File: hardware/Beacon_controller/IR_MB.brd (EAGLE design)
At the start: 50.8 x 50.8 mm, 9 parts, among them U1 ATTINY84ATTINY84-20MU

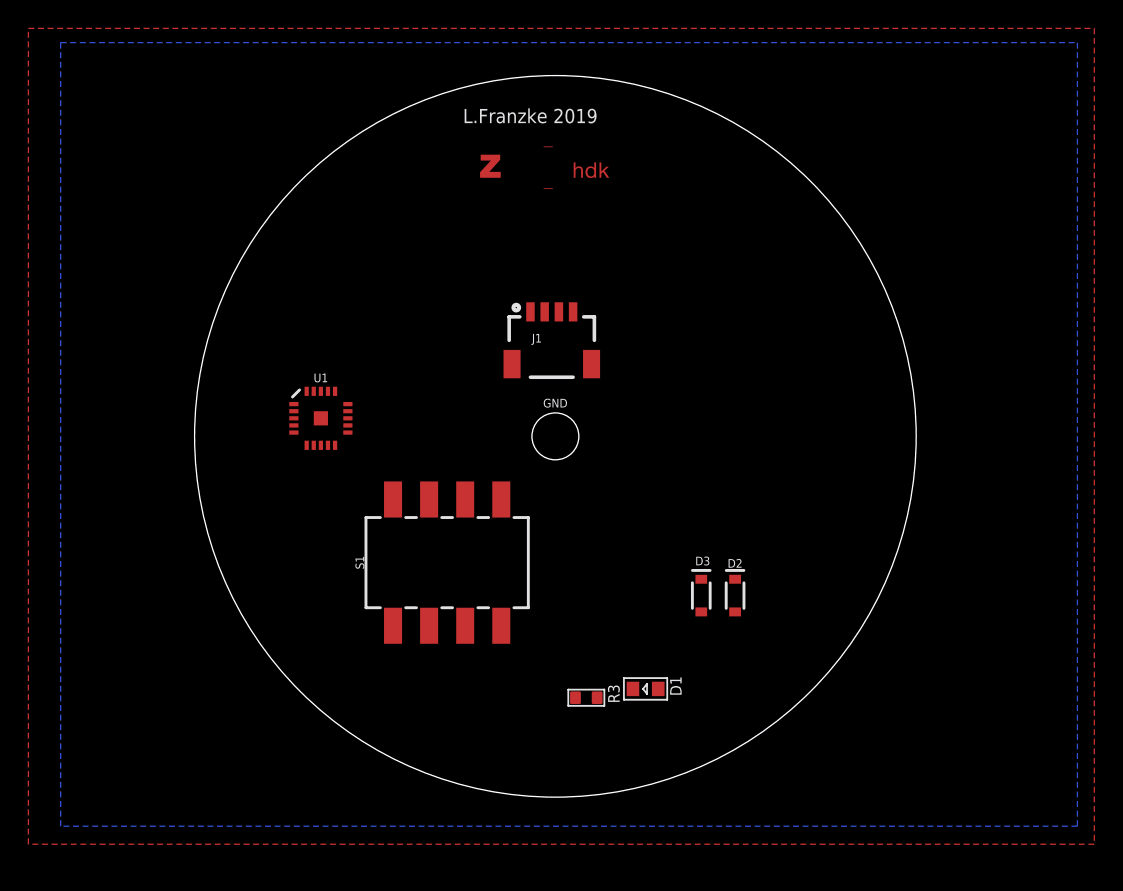
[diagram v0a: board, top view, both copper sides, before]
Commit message: Finished Cad files for beacon, and added new 5 bit patern for markers.
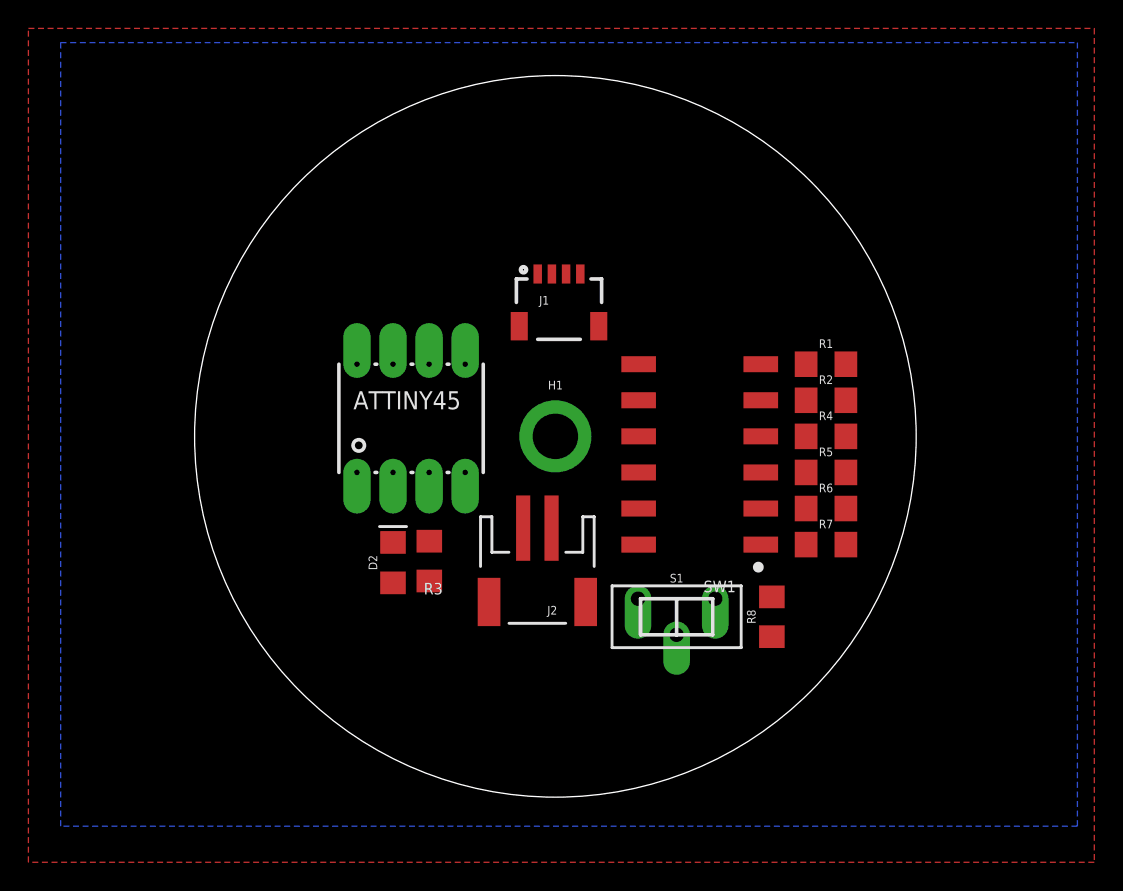
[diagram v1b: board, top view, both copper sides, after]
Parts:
- removed D1: red, Discrete:LED0603
- removed D3: 250mA/100V, SparkFun-DiscreteSemi:SOD-323
- removed GND: STAND-OFF, SparkFun-Hardware:STAND-OFF
- removed U$2: (no value), IAD_GRAPHIC:ZHDK_LOGO
- removed U1: ATTINY84ATTINY84-20MU, SparkFun-IC-Microcontroller:QFN20
- added H1: STANDOFF_ELECTRICAL, IAD-Library:STANDOFF-ELECTRICAL
- added J2: (no value), SparkFun-Connectors:JST-2-SMD
- added R1, R2, R4, R5, R6, R7, R8: 10, SparkFun-Resistors:1206
- added SW1: DIP-06, SparkFun-Switches:DIPSWITCH-06-SMD
- added U$1: ATTINY45, IAD-Library:8PDIP
- D2: value 250mA/100V -> (none); device SparkFun-DiscreteSemi:SOD-323 -> SparkFun-LED:FKIT-LED-1206
- R3: value 150 -> 10; device Discrete:0603_S -> SparkFun-Resistors:1206
- S1: value DIP-04SMD -> (none); device SparkFun-Switches:DIPSWITCH-04-SMD -> SparkFun-Switches:SWITCH_SPDT_PTH_11.6X4.0MM_KIT
- moved D2 24.2 mm to (24.1, 11.4), turned to 90 degrees
- moved S1 16.6 mm to (44.1, 7.62), turned to 270 degrees
- moved R3 14.7 mm to (26.7, 11.5), turned to 90 degrees
- moved J1 2.71 mm to (35.8, 31.8)
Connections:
- removed net 1: J1.1
- removed net 2: J1.2
- new net 3.3V: J1.2, S1.1, SW1.10, SW1.11, SW1.12, SW1.7, SW1.8, SW1.9, U$1.P$8
- new net ADC1: R1.2, R2.2, R4.2, R5.2, R6.2, R7.2, R8.2, U$1.P$7
- new net GND: D2.C, H1.P1, J1.1, J2.1, R8.1, U$1.P$4
- new net N$10: R6.1, SW1.2
- new net N$11: R7.1, SW1.1
- new net N$3: J1.4, U$1.P$5
- new net N$4: J1.3, U$1.P$6
- new net N$5: J2.2, S1.2
- new net N$8: R4.1, SW1.4
- net N$1: now also U$1.P$3
- net N$2: now also D2.A; no longer D1.1
- net N$6: now also R1.1, SW1.6; no longer D2.A
- net N$7: now also R2.1, SW1.5; no longer D3.A
- net N$9: now also R5.1, SW1.3; no longer D2.C, D3.C
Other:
- board text removed: "L.Franzke 2019"

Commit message: Added Multitouch Demo
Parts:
- moved J2 2.54 mm to (34.3, 7.62)
- moved J1 1.27 mm to (35.8, 33.0)
- moved S1 1.27 mm to (44.1, 6.35)
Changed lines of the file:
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@@
 <?xml version="1.0" encoding="utf-8"?>
 <!DOCTYPE eagle SYSTEM "eagle.dtd">
-<eagle version="9.4.2">
+<eagle version="9.2.2">
 <drawing>
 <settings>
@@
 <attribute name="VALUE" value="10" x="26.685" y="11.539" size="1.778" layer="27" rot="R90" display="off"/>
 </element>
-<element name="J1" library="SparkFun-Connectors" package="1X04_1MM_RA" value="" x="35.814" y="31.75" smashed="yes">
-<attribute name="NAME" x="34.417" y="29.591" size="0.6096" layer="25" font="vector" ratio="20"/>
-<attribute name="PROD_ID" value="CONN-13694" x="35.814" y="31.75" size="1.778" layer="27" font="vector" ratio="15" display="off"/>
-<attribute name="VALUE" x="34.163" y="28.448" size="0.6096" layer="27" font="vector" ratio="20"/>
+<element name="J1" library="SparkFun-Connectors" package="1X04_1MM_RA" value="" x="35.814" y="33.02" smashed="yes">
+<attribute name="NAME" x="34.417" y="30.861" size="0.6096" layer="25" font="vector" ratio="20"/>
+<attribute name="PROD_ID" value="CONN-13694" x="35.814" y="33.02" size="1.778" layer="27" font="vector" ratio="15" display="off"/>
+<attribute name="VALUE" x="34.163" y="29.718" size="0.6096" layer="27" font="vector" ratio="20"/>
 </element>
 <element name="U$1" library="IAD-Library" package="8PDIP" value="ATTINY45" x="25.4" y="21.59" smashed="yes"/>
@@
 <attribute name="VALUE" x="51.943" y="7.62" size="0.6096" layer="27" font="vector" ratio="20" rot="R90" align="top-center"/>
 </element>
-<element name="S1" library="SparkFun-Switches" package="SWITCH_SPDT_PTH_11.6X4.0MM_KIT" value="" x="44.0944" y="7.62" smashed="yes" rot="R270">
-<attribute name="NAME" x="44.0944" y="10.033" size="0.6096" layer="25" font="vector" ratio="20" align="bottom-center"/>
-<attribute name="PROD_ID" value="SWCH-08261" x="44.0944" y="7.62" size="1.778" layer="27" font="vector" ratio="15" rot="R270" display="off"/>
-<attribute name="SF_SKU" value="COM-00102" x="44.0944" y="7.62" size="1.778" layer="27" font="vector" ratio="15" rot="R270" display="off"/>
-<attribute name="VALUE" x="44.0944" y="5.207" size="0.6096" layer="27" font="vector" ratio="20" align="top-center"/>
-</element>
-<element name="J2" library="SparkFun-Connectors" package="JST-2-SMD" value="" x="34.29" y="10.16" smashed="yes" rot="R180">
-<attribute name="NAME" x="35.687" y="8.382" size="0.6096" layer="25" font="vector" ratio="20" rot="R180"/>
-<attribute name="PROD_ID" value="CONN-11443" x="34.29" y="10.16" size="1.778" layer="27" font="vector" ratio="15" rot="R180" display="off"/>
-<attribute name="SF_ID" value="PRT-08612" x="34.29" y="10.16" size="1.778" layer="27" font="vector" ratio="15" rot="R180" display="off"/>
-<attribute name="VALUE" x="35.941" y="9.525" size="0.6096" layer="27" font="vector" ratio="20" rot="R180"/>
+<element name="S1" library="SparkFun-Switches" package="SWITCH_SPDT_PTH_11.6X4.0MM_KIT" value="" x="44.0944" y="6.35" smashed="yes" rot="R270">
+<attribute name="NAME" x="44.0944" y="8.763" size="0.6096" layer="25" font="vector" ratio="20" align="bottom-center"/>
+<attribute name="PROD_ID" value="SWCH-08261" x="44.0944" y="6.35" size="1.778" layer="27" font="vector" ratio="15" rot="R270" display="off"/>
+<attribute name="SF_SKU" value="COM-00102" x="44.0944" y="6.35" size="1.778" layer="27" font="vector" ratio="15" rot="R270" display="off"/>
+<attribute name="VALUE" x="44.0944" y="3.937" size="0.6096" layer="27" font="vector" ratio="20" align="top-center"/>
+</element>
+<element name="J2" library="SparkFun-Connectors" package="JST-2-SMD" value="" x="34.29" y="7.62" smashed="yes" rot="R180">
+<attribute name="NAME" x="35.687" y="5.842" size="0.6096" layer="25" font="vector" ratio="20" rot="R180"/>
+<attribute name="PROD_ID" value="CONN-11443" x="34.29" y="7.62" size="1.778" layer="27" font="vector" ratio="15" rot="R180" display="off"/>
+<attribute name="SF_ID" value="PRT-08612" x="34.29" y="7.62" size="1.778" layer="27" font="vector" ratio="15" rot="R180" display="off"/>
+<attribute name="VALUE" x="35.941" y="6.985" size="0.6096" layer="27" font="vector" ratio="20" rot="R180"/>
 </element>
 <element name="D2" library="SparkFun-LED" package="FKIT-LED-1206" value="" x="24.13" y="11.43" smashed="yes" rot="R90">
@@
 <contactref element="J2" pad="1"/>
 <contactref element="D2" pad="C"/>
-<wire x1="35.56" y1="20.32" x2="34.314" y2="31.75" width="0" layer="19" extent="1-1"/>
+<wire x1="35.56" y1="20.32" x2="34.314" y2="33.02" width="0" layer="19" extent="1-1"/>
 <wire x1="29.21" y1="17.78" x2="35.56" y2="20.32" width="0" layer="19" extent="1-1"/>
-<wire x1="35.29" y1="13.86" x2="35.56" y2="20.32" width="0" layer="19" extent="1-1"/>
-<wire x1="50.8" y1="6.22" x2="35.29" y2="13.86" width="0" layer="19" extent="1-1"/>
+<wire x1="35.29" y1="11.32" x2="35.56" y2="20.32" width="0" layer="19" extent="1-1"/>
+<wire x1="50.8" y1="6.22" x2="35.29" y2="11.32" width="0" layer="19" extent="1-1"/>
 <wire x1="24.13" y1="12.852" x2="29.21" y2="17.78" width="0" layer="19" extent="1-1"/>
 </signal>
@@
 <contactref element="SW1" pad="7"/>
 <contactref element="S1" pad="1"/>
-<wire x1="41.42" y1="25.4" x2="35.314" y2="31.75" width="0" layer="19" extent="1-1"/>
+<wire x1="41.42" y1="25.4" x2="35.314" y2="33.02" width="0" layer="19" extent="1-1"/>
 <wire x1="41.42" y1="22.86" x2="41.42" y2="25.4" width="0" layer="19" extent="1-1"/>
 <wire x1="41.42" y1="20.32" x2="41.42" y2="22.86" width="0" layer="19" extent="1-1"/>
@@
 <wire x1="41.42" y1="15.24" x2="41.42" y2="17.78" width="0" layer="19" extent="1-1"/>
 <wire x1="41.42" y1="12.7" x2="41.42" y2="15.24" width="0" layer="19" extent="1-1"/>
-<wire x1="46.8122" y1="8.89" x2="41.42" y2="12.7" width="0" layer="19" extent="1-1"/>
-<wire x1="21.59" y1="25.4" x2="35.314" y2="31.75" width="0" layer="19" extent="1-1"/>
+<wire x1="46.8122" y1="7.62" x2="41.42" y2="12.7" width="0" layer="19" extent="1-1"/>
+<wire x1="21.59" y1="25.4" x2="35.314" y2="33.02" width="0" layer="19" extent="1-1"/>
 </signal>
 <signal name="N$3">
 <contactref element="J1" pad="4"/>
 <contactref element="U$1" pad="P$5"/>
-<wire x1="29.21" y1="25.4" x2="37.314" y2="31.75" width="0" layer="19" extent="1-1"/>
+<wire x1="29.21" y1="25.4" x2="37.314" y2="33.02" width="0" layer="19" extent="1-1"/>
 </signal>
 <signal name="N$4">
 <contactref element="J1" pad="3"/>
 <contactref element="U$1" pad="P$6"/>
-<wire x1="26.67" y1="25.4" x2="36.314" y2="31.75" width="0" layer="19" extent="1-1"/>
+<wire x1="26.67" y1="25.4" x2="36.314" y2="33.02" width="0" layer="19" extent="1-1"/>
 </signal>
 <signal name="N$6">
@@
 <contactref element="J2" pad="2"/>
 <contactref element="S1" pad="2"/>
-<wire x1="44.0944" y1="6.35" x2="33.29" y2="13.86" width="0" layer="19" extent="1-1"/>
+<wire x1="44.0944" y1="5.08" x2="33.29" y2="11.32" width="0" layer="19" extent="1-1"/>
 </signal>
 </signals>
